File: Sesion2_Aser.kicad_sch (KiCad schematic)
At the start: 0 parts

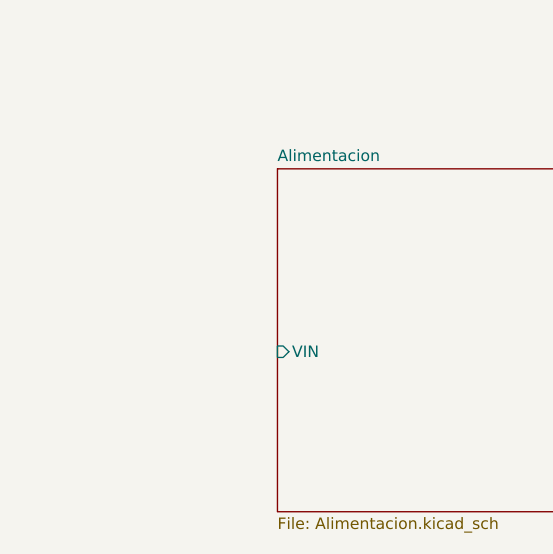
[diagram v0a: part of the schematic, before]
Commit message: Alimentacion: J101 bornas 9 V, U201 MCP1703A 3,3 V, C201/C202 1 uF (huellas y MPN)
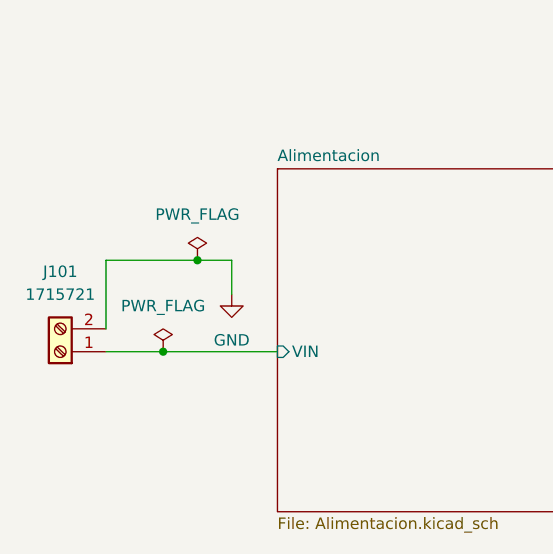
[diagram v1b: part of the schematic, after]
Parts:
- added J101: 1715721, TerminalBlock_Phoenix:TerminalBlock_Phoenix_MKDS-1,5-2-5.08_1x02_P5.08mm_Horizontal, symbol Connector:Screw_Terminal_01x02
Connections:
- net Alimentacion/VIN: now also J101.1 (Pin_1)
- new net GND: J101.2 (Pin_2)

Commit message: Correcciones: huella C202, conectores J301/J302, SWD al MCU, MPN en su campo y BOM
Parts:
- J101: MPN (none) -> 1715721; Manufacturer (none) -> Phoenix Contact
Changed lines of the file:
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@@
 			)
 		)
-		(property "MPN" ""
+		(property "MPN" "1715721"
 			(at 16.51 147.32 0)
 			(hide yes)
@@
 			)
 		)
-		(property "Manufacturer" ""
+		(property "Manufacturer" "Phoenix Contact"
 			(at 16.51 147.32 0)
 			(hide yes)

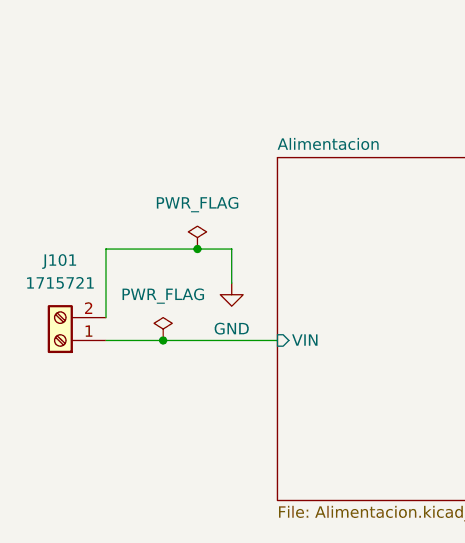
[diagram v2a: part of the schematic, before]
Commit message: Valores eléctricos en Value y BOM actualizada
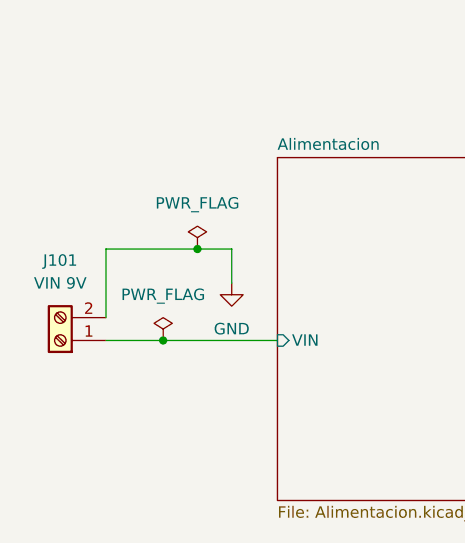
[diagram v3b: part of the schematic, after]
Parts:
- J101: value 1715721 -> VIN 9V
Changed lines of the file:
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@@
 			)
 		)
-		(property "Value" "1715721"
+		(property "Value" "VIN 9V"
 			(at 16.51 140.97 0)
 			(show_name no)
